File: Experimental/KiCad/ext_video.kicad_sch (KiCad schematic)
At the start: 30 parts, among them IC13 RT9742SNGV, IC14 TPD4E001DRLR, IC15 TPD4E001DRLR, IC16 TPD12S016PWR, IC17 MIC2026A-1YM-TR, IC18 TPD4E001DRLR, X7 0862-1J1T-43-F, X8 SS-53000-002, X9 5051102091

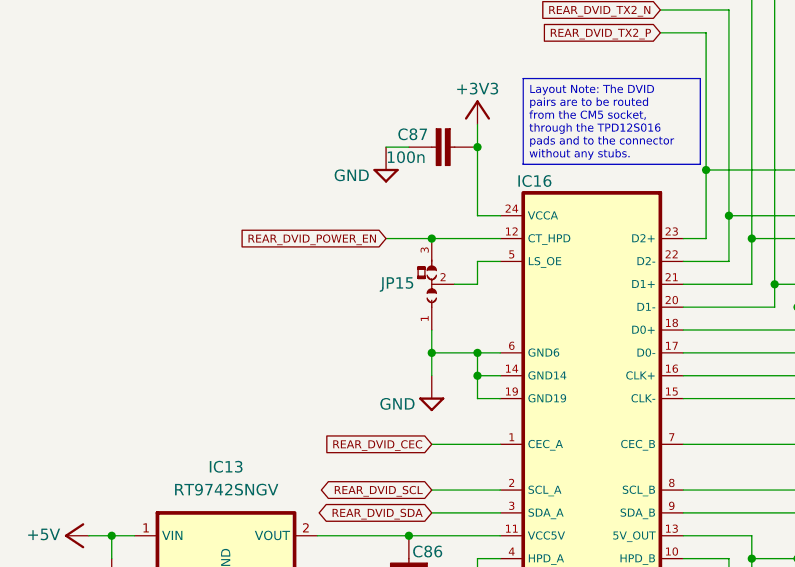
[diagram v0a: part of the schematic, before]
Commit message: BOM update, small changes
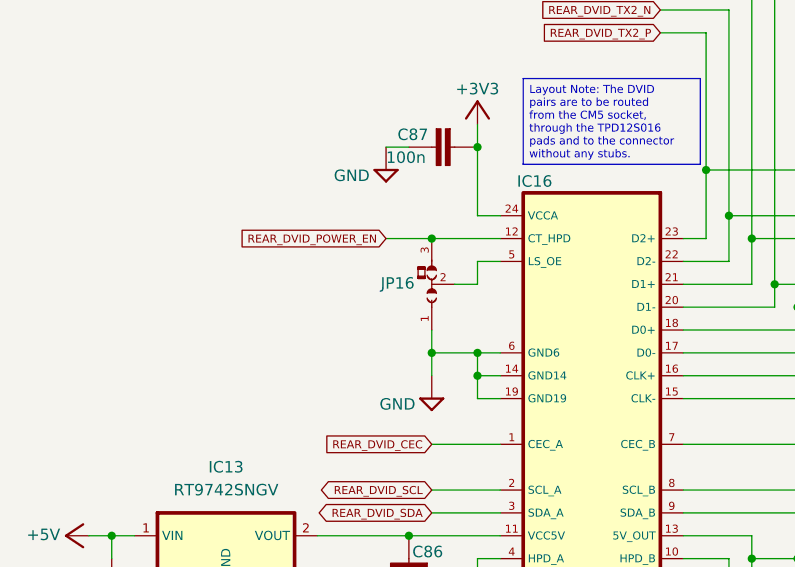
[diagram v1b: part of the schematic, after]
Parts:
- IC14, IC15, IC18: TME - -> TPD4E001DRLR
- X8: DigiKey 609-4614-1-ND -> 380-SS-53000-002-ND; Mouser 649-10029449-111RLF -> 530-SS-53000-002; TME 10029449-111RLF -> -
- renumbered JP15 to JP16
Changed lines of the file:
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@@
 	(title_block
 		(title "BB3+ test mainboard")
-		(date "2025-10-11")
+		(date "2025-10-12")
 		(rev "r1B1")
 		(company "Envox d.o.o.")
@@
 		(on_board yes)
 		(dnp no)
-		(property "Reference" "#SUPPLY052"
+		(property "Reference" "#SUPPLY053"
 			(at 71.12 68.58 0)
 			(effects
@@
 			(project "BB3plus MCU test board"
 				(path "/1df84e4f-233a-4f72-9418-c0020706bb76/c0a485a3-023d-4313-ae06-c16e1fdbf75a"
-					(reference "#SUPPLY052")
+					(reference "#SUPPLY053")
 					(unit 1)
 				)
@@
 			)
 		)
-		(property "TME" "-"
+		(property "TME" "TPD4E001DRLR"
 			(at 63.5 38.1 0)
 			(show_name yes)
@@
 		(on_board yes)
 		(dnp no)
-		(property "Reference" "#SUPPLY051"
+		(property "Reference" "#SUPPLY052"
 			(at 38.1 68.58 0)
 			(effects
@@
 			(project "BB3plus MCU test board"
 				(path "/1df84e4f-233a-4f72-9418-c0020706bb76/c0a485a3-023d-4313-ae06-c16e1fdbf75a"
-					(reference "#SUPPLY051")
+					(reference "#SUPPLY052")
 					(unit 1)
 				)
@@
 			)
 		)
-		(property "DigiKey" "609-4614-1-ND"
+		(property "DigiKey" "380-SS-53000-002-ND"
 			(at 116.84 188.722 0)
 			(effects
@@
 			)
 		)
-		(property "Mouser" "649-10029449-111RLF"
+		(property "Mouser" " 530-SS-53000-002"
 			(at 116.84 186.436 0)
 			(effects
@@
 			)
 		)
-		(property "TME" "10029449-111RLF"
+		(property "TME" "-"
 			(at 117.348 191.008 0)
 			(effects
@@
 		(on_board yes)
 		(dnp no)
-		(property "Reference" "#SUPPLY055"
+		(property "Reference" "#SUPPLY056"
 			(at 271.78 58.42 0)
 			(effects
@@
 			(project "BB3plus MCU test board"
 				(path "/1df84e4f-233a-4f72-9418-c0020706bb76/c0a485a3-023d-4313-ae06-c16e1fdbf75a"
-					(reference "#SUPPLY055")
+					(reference "#SUPPLY056")
 					(unit 1)
 				)
@@
 		(on_board yes)
 		(dnp no)
-		(property "Reference" "#SUPPLY054"
+		(property "Reference" "#SUPPLY055"
 			(at 91.44 91.44 0)
 			(effects
@@
 			(project "BB3plus MCU test board"
 				(path "/1df84e4f-233a-4f72-9418-c0020706bb76/c0a485a3-023d-4313-ae06-c16e1fdbf75a"
-					(reference "#SUPPLY054")
+					(reference "#SUPPLY055")
 					(unit 1)
 				)
@@
 			)
 		)
-		(property "TME" "-"
+		(property "TME" "TPD4E001DRLR"
 			(at 261.62 63.5 0)
 			(show_name yes)
@@
 		(on_board yes)
 		(dnp no)
-		(property "Reference" "JP15"
+		(property "Reference" "JP16"
 			(at 56.515 145.415 90)
 			(effects
@@
 			(project "BB3plus MCU test board"
 				(path "/1df84e4f-233a-4f72-9418-c0020706bb76/c0a485a3-023d-4313-ae06-c16e1fdbf75a"
-					(reference "JP15")
+					(reference "JP16")
 					(unit 1)
 				)
@@
 			)
 		)
-		(property "TME" "-"
+		(property "TME" "TPD4E001DRLR"
 			(at 48.26 76.2 0)
 			(show_name yes)
@@
 		(on_board yes)
 		(dnp no)
-		(property "Reference" "#SUPPLY053"
+		(property "Reference" "#SUPPLY054"
 			(at 73.66 33.02 0)
 			(effects
@@
 			(project "BB3plus MCU test board"
 				(path "/1df84e4f-233a-4f72-9418-c0020706bb76/c0a485a3-023d-4313-ae06-c16e1fdbf75a"
-					(reference "#SUPPLY053")
+					(reference "#SUPPLY054")
 					(unit 1)
 				)

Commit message: AC/DC module replaced with 45/60W model
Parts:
- X8: Label (none) -> Ext DVID
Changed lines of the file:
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@@
+			)
+		)
+		(property "Label" "Ext DVID"
+			(at 116.84 154.94 0)
+			(effects
+				(font
+					(size 0.889 0.889)
+				)
+				(hide yes)
 			)
 		)

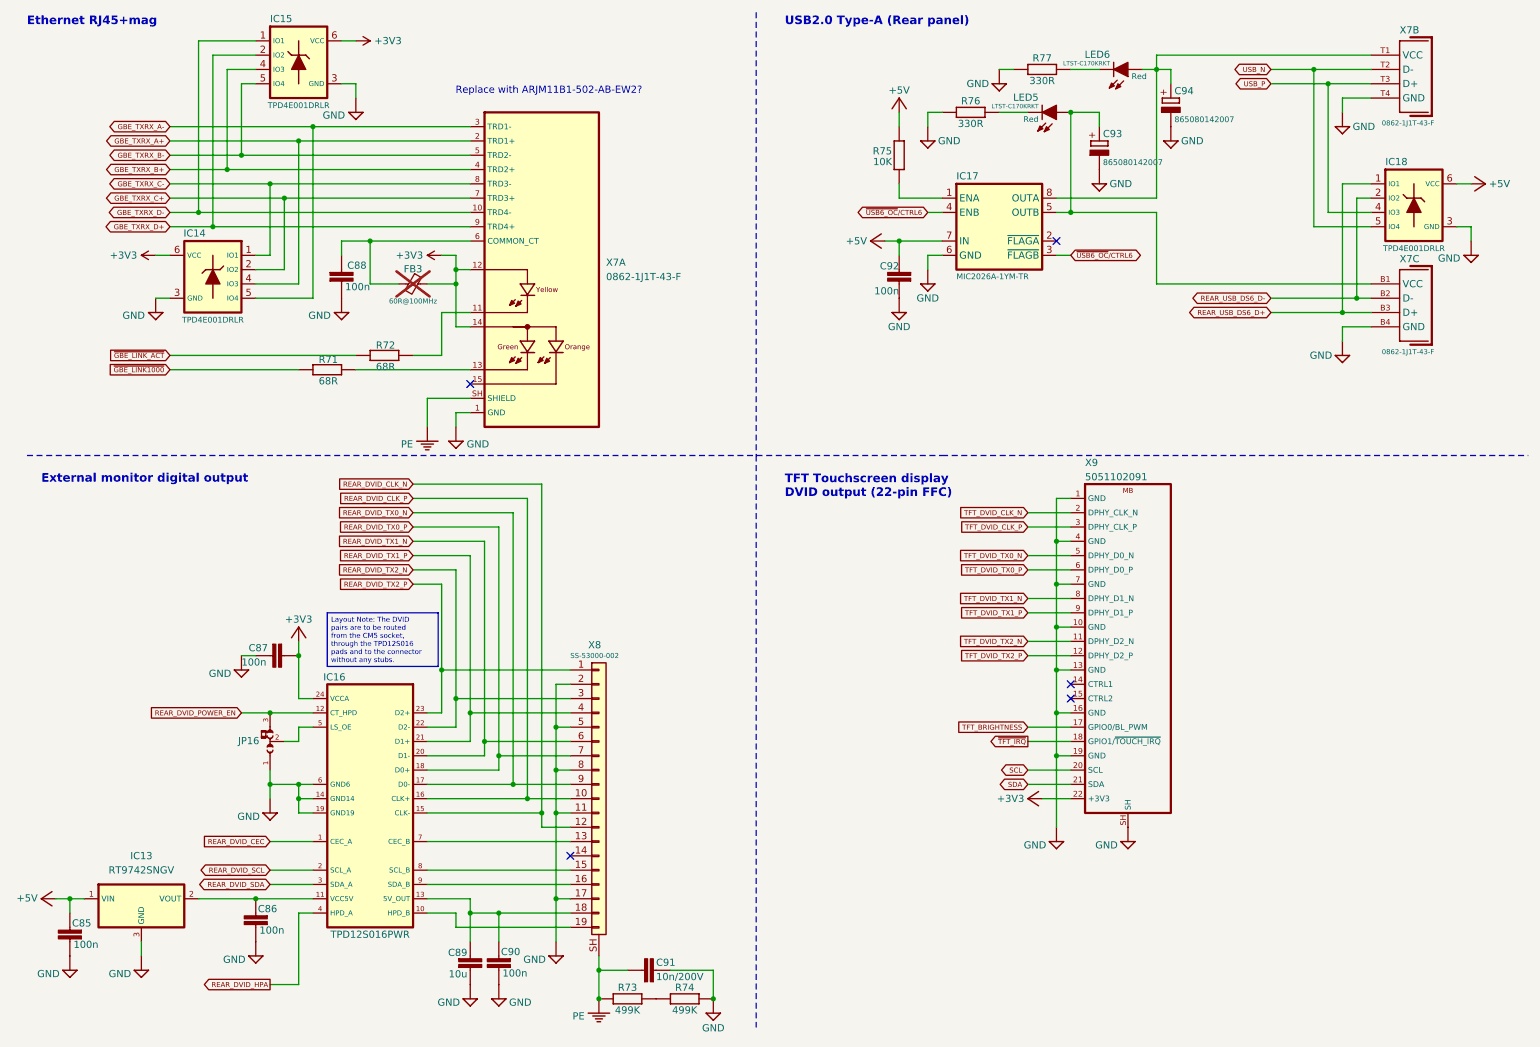
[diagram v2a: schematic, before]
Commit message: Replace 5V buck with 6A low EMI version
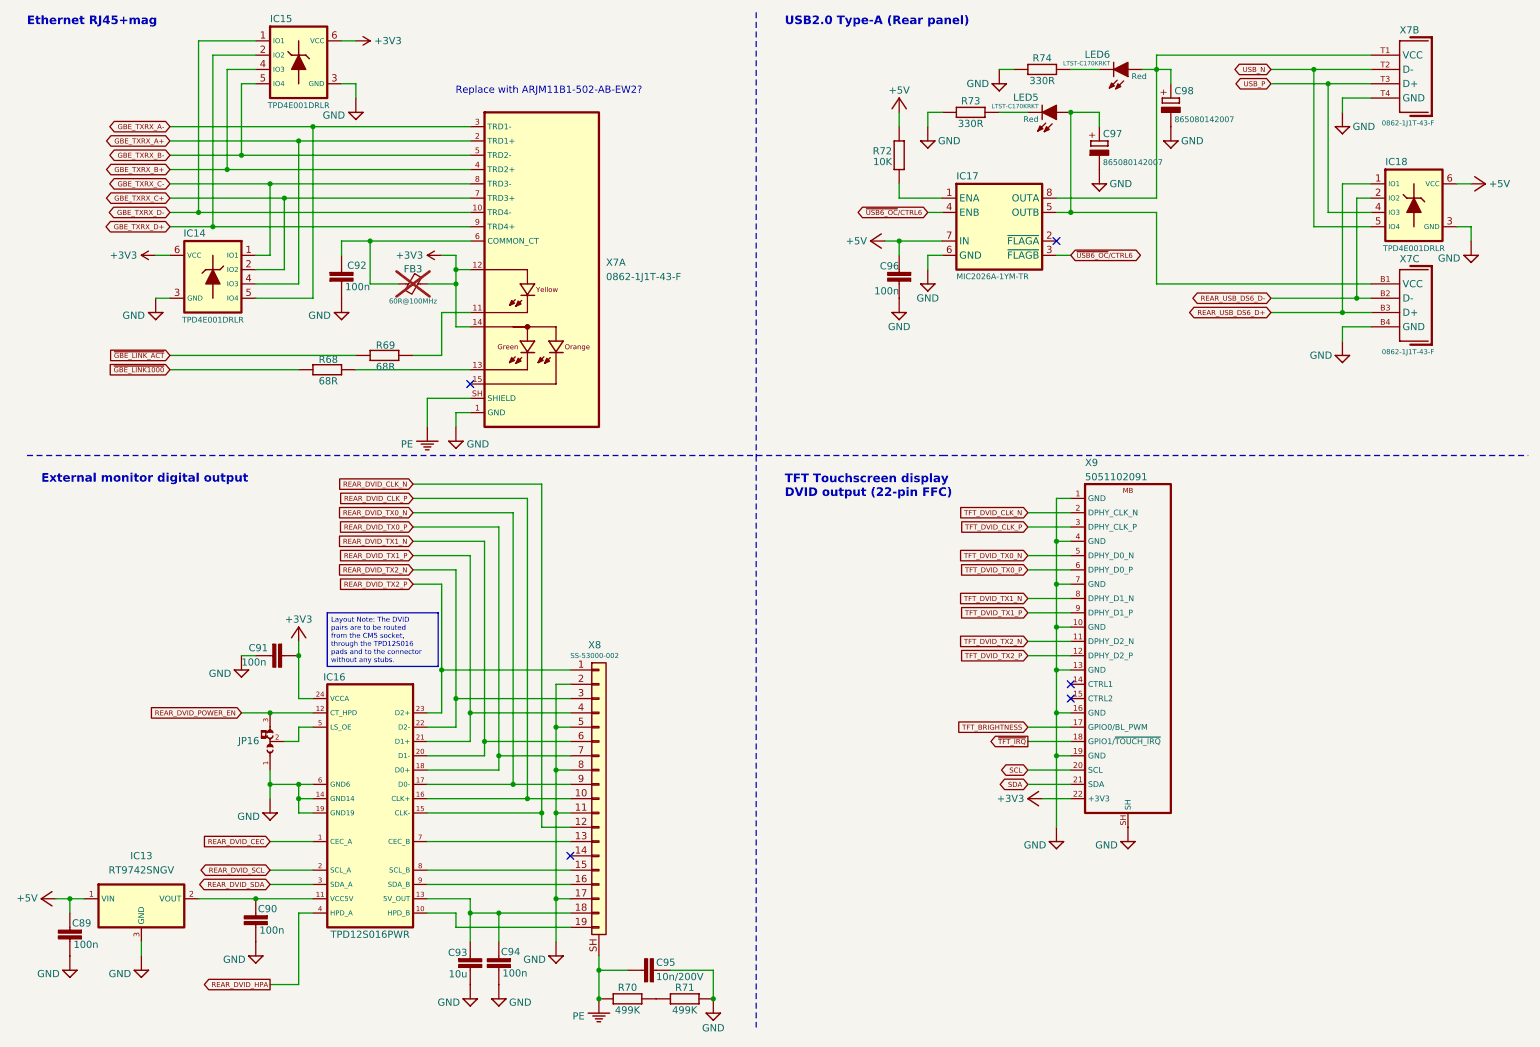
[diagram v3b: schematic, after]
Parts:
- renumbered C85 to C89, C86 to C90, C87 to C91, C88 to C92, C89 to C93, C90 to C94, C91 to C95, C92 to C96, C93 to C97, C94 to C98, R71 to R68, R72 to R69, R73 to R70, R74 to R71, R75 to R72, R76 to R73, R77 to R74
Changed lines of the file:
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@@
 		(on_board yes)
 		(dnp no)
-		(property "Reference" "R77"
+		(property "Reference" "R74"
 			(at 195.58 24.13 90)
 			(effects
@@
 			(project "BB3plus MCU test board"
 				(path "/1df84e4f-233a-4f72-9418-c0020706bb76/c0a485a3-023d-4313-ae06-c16e1fdbf75a"
-					(reference "R77")
+					(reference "R74")
 					(unit 1)
 				)
@@
 		(on_board yes)
 		(dnp no)
-		(property "Reference" "#SUPPLY053"
+		(property "Reference" "#SUPPLY055"
 			(at 71.12 68.58 0)
 			(effects
@@
 			(project "BB3plus MCU test board"
 				(path "/1df84e4f-233a-4f72-9418-c0020706bb76/c0a485a3-023d-4313-ae06-c16e1fdbf75a"
-					(reference "#SUPPLY053")
+					(reference "#SUPPLY055")
 					(unit 1)
 				)
@@
 		(on_board yes)
 		(dnp no)
-		(property "Reference" "C87"
+		(property "Reference" "C91"
 			(at 54.61 128.905 90)
 			(effects
@@
 			(project "BB3plus MCU test board"
 				(path "/1df84e4f-233a-4f72-9418-c0020706bb76/c0a485a3-023d-4313-ae06-c16e1fdbf75a"
-					(reference "C87")
+					(reference "C91")
 					(unit 1)
 				)
@@
 		(on_board yes)
 		(dnp no)
-		(property "Reference" "R76"
+		(property "Reference" "R73"
 			(at 182.88 31.75 90)
 			(effects
@@
 			(project "BB3plus MCU test board"
 				(path "/1df84e4f-233a-4f72-9418-c0020706bb76/c0a485a3-023d-4313-ae06-c16e1fdbf75a"
-					(reference "R76")
+					(reference "R73")
 					(unit 1)
 				)
@@
 		(on_board yes)
 		(dnp no)
-		(property "Reference" "C93"
+		(property "Reference" "C97"
 			(at 206.375 36.83 0)
 			(effects
@@
 			(project "BB3plus MCU test board"
 				(path "/1df84e4f-233a-4f72-9418-c0020706bb76/c0a485a3-023d-4313-ae06-c16e1fdbf75a"
-					(reference "C93")
+					(reference "C97")
 					(unit 1)
 				)
@@
 		(on_board yes)
 		(dnp no)
-		(property "Reference" "#SUPPLY052"
+		(property "Reference" "#SUPPLY054"
 			(at 38.1 68.58 0)
 			(effects
@@
 			(project "BB3plus MCU test board"
 				(path "/1df84e4f-233a-4f72-9418-c0020706bb76/c0a485a3-023d-4313-ae06-c16e1fdbf75a"
-					(reference "#SUPPLY052")
+					(reference "#SUPPLY054")
 					(unit 1)
 				)
@@
 		(on_board yes)
 		(dnp no)
-		(property "Reference" "R75"
+		(property "Reference" "R72"
 			(at 168.91 40.64 0)
 			(effects
@@
 			(project "BB3plus MCU test board"
 				(path "/1df84e4f-233a-4f72-9418-c0020706bb76/c0a485a3-023d-4313-ae06-c16e1fdbf75a"
-					(reference "R75")
+					(reference "R72")
 					(unit 1)
 				)
@@
 		(on_board yes)
 		(dnp no)
-		(property "Reference" "C85"
+		(property "Reference" "C89"
 			(at 26.67 177.8 0)
 			(effects
@@
 			(project "BB3plus MCU test board"
 				(path "/1df84e4f-233a-4f72-9418-c0020706bb76/c0a485a3-023d-4313-ae06-c16e1fdbf75a"
-					(reference "C85")
+					(reference "C89")
 					(unit 1)
 				)
@@
 		(on_board yes)
 		(dnp no)
-		(property "Reference" "R74"
+		(property "Reference" "R71"
 			(at 132.08 189.23 90)
 			(effects
@@
 			(project "BB3plus MCU test board"
 				(path "/1df84e4f-233a-4f72-9418-c0020706bb76/c0a485a3-023d-4313-ae06-c16e1fdbf75a"
-					(reference "R74")
+					(reference "R71")
 					(unit 1)
 				)
@@
 		(on_board yes)
 		(dnp no)
-		(property "Reference" "#SUPPLY056"
+		(property "Reference" "#SUPPLY058"
 			(at 271.78 58.42 0)
 			(effects
@@
 			(project "BB3plus MCU test board"
 				(path "/1df84e4f-233a-4f72-9418-c0020706bb76/c0a485a3-023d-4313-ae06-c16e1fdbf75a"
-					(reference "#SUPPLY056")
+					(reference "#SUPPLY058")
 					(unit 1)
 				)
@@
 		(on_board yes)
 		(dnp no)
-		(property "Reference" "R71"
+		(property "Reference" "R68"
 			(at 70.485 76.2 90)
 			(effects
@@
 			(project "BB3plus MCU test board"
 				(path "/1df84e4f-233a-4f72-9418-c0020706bb76/c0a485a3-023d-4313-ae06-c16e1fdbf75a"
-					(reference "R71")
+					(reference "R68")
 					(unit 1)
 				)
@@
 		(on_board yes)
 		(dnp no)
-		(property "Reference" "C89"
+		(property "Reference" "C93"
 			(at 93.472 183.0324 0)
 			(effects
@@
 			(project "BB3plus MCU test board"
 				(path "/1df84e4f-233a-4f72-9418-c0020706bb76/c0a485a3-023d-4313-ae06-c16e1fdbf75a"
-					(reference "C89")
+					(reference "C93")
 					(unit 1)
 				)
@@
 		(on_board yes)
 		(dnp no)
-		(property "Reference" "#SUPPLY055"
+		(property "Reference" "#SUPPLY057"
 			(at 91.44 91.44 0)
 			(effects
@@
 			(project "BB3plus MCU test board"
 				(path "/1df84e4f-233a-4f72-9418-c0020706bb76/c0a485a3-023d-4313-ae06-c16e1fdbf75a"
-					(reference "#SUPPLY055")
+					(reference "#SUPPLY057")
 					(unit 1)
 				)
@@
 		(on_board yes)
 		(dnp no)
-		(property "Reference" "C90"
+		(property "Reference" "C94"
 			(at 102.87 182.88 0)
 			(effects
@@
 			(project "BB3plus MCU test board"
 				(path "/1df84e4f-233a-4f72-9418-c0020706bb76/c0a485a3-023d-4313-ae06-c16e1fdbf75a"
-					(reference "C90")
+					(reference "C94")
 					(unit 1)
 				)
@@
 		(on_board yes)
 		(dnp no)
-		(property "Reference" "C86"
+		(property "Reference" "C90"
 			(at 59.69 175.26 0)
 			(effects
@@
 			(project "BB3plus MCU test board"
 				(path "/1df84e4f-233a-4f72-9418-c0020706bb76/c0a485a3-023d-4313-ae06-c16e1fdbf75a"
-					(reference "C86")
+					(reference "C90")
 					(unit 1)
 				)
@@
 		(on_board yes)
 		(dnp no)
-		(property "Reference" "C88"
+		(property "Reference" "C92"
 			(at 75.565 60.96 0)
 			(effects
@@
 			(project "BB3plus MCU test board"
 				(path "/1df84e4f-233a-4f72-9418-c0020706bb76/c0a485a3-023d-4313-ae06-c16e1fdbf75a"
-					(reference "C88")
+					(reference "C92")
 					(unit 1)
 				)
@@
 		(on_board yes)
 		(dnp no)
-		(property "Reference" "R73"
+		(property "Reference" "R70"
 			(at 121.92 189.23 90)
 			(effects
@@
 			(project "BB3plus MCU test board"
 				(path "/1df84e4f-233a-4f72-9418-c0020706bb76/c0a485a3-023d-4313-ae06-c16e1fdbf75a"
-					(reference "R73")
+					(reference "R70")
 					(unit 1)
 				)
@@
 		(on_board yes)
 		(dnp no)
-		(property "Reference" "R72"
+		(property "Reference" "R69"
 			(at 80.645 73.66 90)
 			(effects
@@
 			(project "BB3plus MCU test board"
 				(path "/1df84e4f-233a-4f72-9418-c0020706bb76/c0a485a3-023d-4313-ae06-c16e1fdbf75a"
-					(reference "R72")
+					(reference "R69")
 					(unit 1)
 				)
@@
 		(on_board yes)
 		(dnp no)
-		(property "Reference" "C92"
+		(property "Reference" "C96"
 			(at 170.18 60.325 0)
 			(effects
@@
 			(project "BB3plus MCU test board"
 				(path "/1df84e4f-233a-4f72-9418-c0020706bb76/c0a485a3-023d-4313-ae06-c16e1fdbf75a"
-					(reference "C92")
+					(reference "C96")
 					(unit 1)
 				)
@@
 		(on_board yes)
 		(dnp no)
-		(property "Reference" "C91"
+		(property "Reference" "C95"
 			(at 127 184.785 90)
 			(effects
@@
 			(project "BB3plus MCU test board"
 				(path "/1df84e4f-233a-4f72-9418-c0020706bb76/c0a485a3-023d-4313-ae06-c16e1fdbf75a"
-					(reference "C91")
+					(reference "C95")
 					(unit 1)
 				)
@@
 		(on_board yes)
 		(dnp no)
-		(property "Reference" "C94"
+		(property "Reference" "C98"
 			(at 219.075 29.21 0)
 			(effects
@@
 			(project "BB3plus MCU test board"
 				(path "/1df84e4f-233a-4f72-9418-c0020706bb76/c0a485a3-023d-4313-ae06-c16e1fdbf75a"
-					(reference "C94")
+					(reference "C98")
 					(unit 1)
 				)
@@
 		(on_board yes)
 		(dnp no)
-		(property "Reference" "#SUPPLY054"
+		(property "Reference" "#SUPPLY056"
 			(at 73.66 33.02 0)
 			(effects
@@
 			(project "BB3plus MCU test board"
 				(path "/1df84e4f-233a-4f72-9418-c0020706bb76/c0a485a3-023d-4313-ae06-c16e1fdbf75a"
-					(reference "#SUPPLY054")
+					(reference "#SUPPLY056")
 					(unit 1)
 				)

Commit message: Update project info
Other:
- company: Envox d.o.o. -> ${project_creator}
- title: BB3+ test mainboard -> ${project_name}
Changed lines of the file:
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@@
 	(paper "A4")
 	(title_block
-		(title "BB3+ test mainboard")
-		(date "2025-10-12")
-		(rev "r1B1")
-		(company "Envox d.o.o.")
-		(comment 1 "Licensed under the TAPR Open Hardware License (www.tapr.org/OHL)")
-		(comment 2 "More info at http://www.envox.eu/")
+		(title "${project_name}")
+		(date "2025-10-13")
+		(rev "${project_version}")
+		(company "${project_creator}")
+		(comment 1 "${project_license}")
+		(comment 2 "${project_info}")
 	)
 	(text "Ethernet RJ45+mag"
